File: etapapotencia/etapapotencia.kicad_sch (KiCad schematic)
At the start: 9 parts

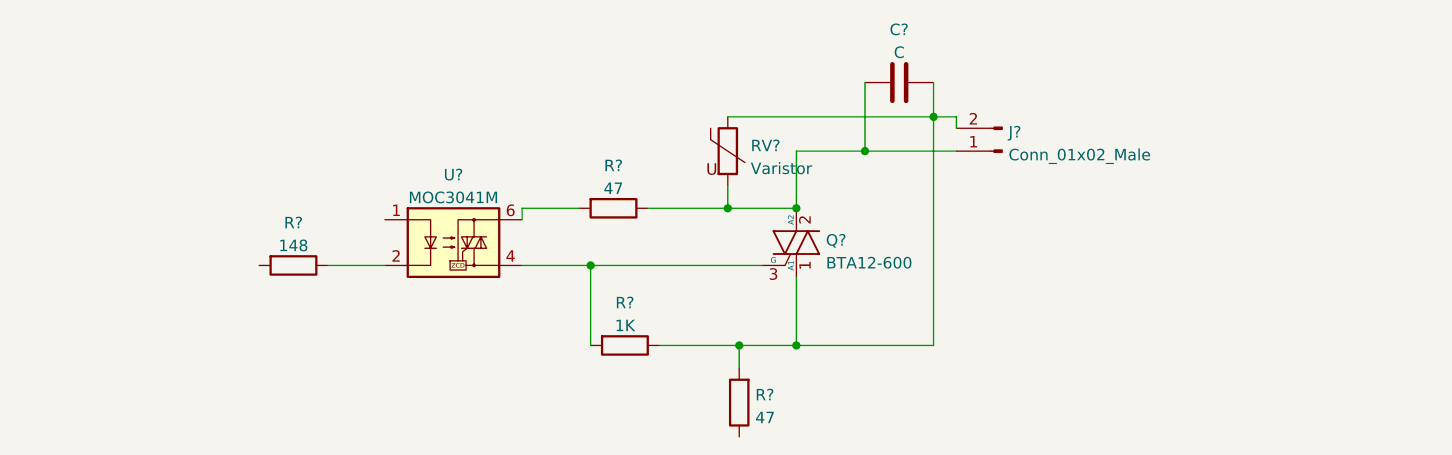
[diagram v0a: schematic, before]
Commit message: Reomo esquemas de etapa de potencia con MOc
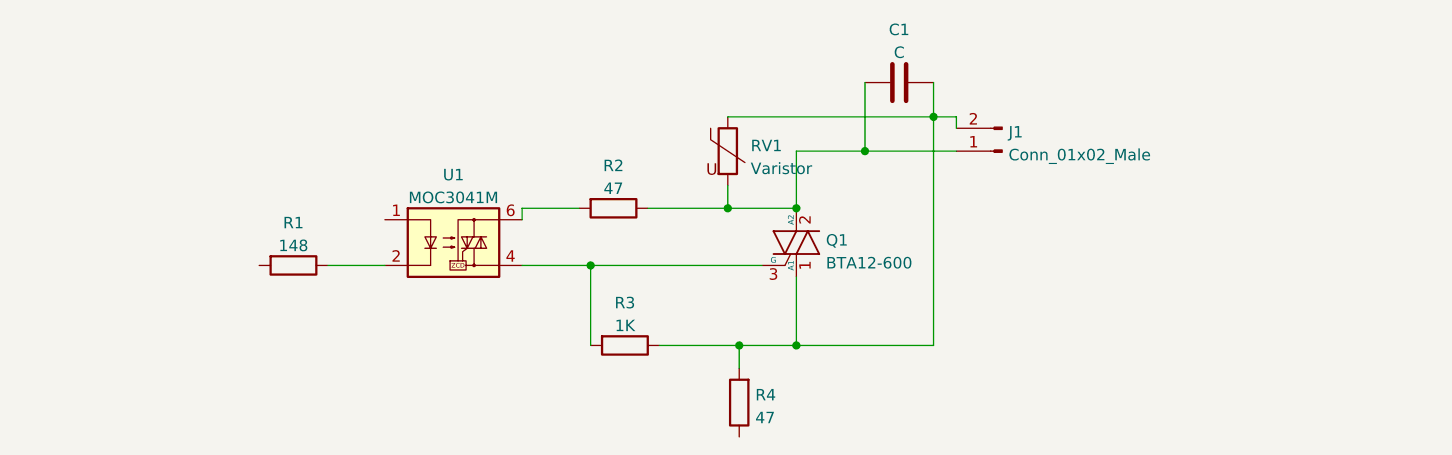
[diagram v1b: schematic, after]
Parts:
- gave numbers to parts that had none: 9
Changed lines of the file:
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@@
   (symbol (lib_id "Device:C") (at 137.16 27.94 90) (unit 1)
     (in_bom yes) (on_board yes) (fields_autoplaced)
-    (property "Reference" "C?" (id 0) (at 137.16 22.0812 90))
+    (property "Reference" "C1" (id 0) (at 137.16 22.0812 90))
     (property "Value" "C" (id 1) (at 137.16 24.6181 90))
     (property "Footprint" "" (id 2) (at 140.97 26.9748 0)
@@
   (symbol (lib_id "Device:R") (at 119.38 63.5 180) (unit 1)
     (in_bom yes) (on_board yes) (fields_autoplaced)
-    (property "Reference" "R?" (id 0) (at 121.158 62.6653 0)
+    (property "Reference" "R4" (id 0) (at 121.158 62.6653 0)
       (effects (font (size 1.27 1.27)) (justify right))
     )
@@
   (symbol (lib_id "Device:R") (at 106.68 57.15 270) (unit 1)
     (in_bom yes) (on_board yes) (fields_autoplaced)
-    (property "Reference" "R?" (id 0) (at 106.68 52.4342 90))
+    (property "Reference" "R3" (id 0) (at 106.68 52.4342 90))
     (property "Value" "1K" (id 1) (at 106.68 54.9711 90))
     (property "Footprint" "" (id 2) (at 106.68 55.372 90)
@@
   (symbol (lib_id "Device:R") (at 105.41 41.91 270) (unit 1)
     (in_bom yes) (on_board yes) (fields_autoplaced)
-    (property "Reference" "R?" (id 0) (at 105.41 37.1942 90))
+    (property "Reference" "R2" (id 0) (at 105.41 37.1942 90))
     (property "Value" "47" (id 1) (at 105.41 39.7311 90))
     (property "Footprint" "" (id 2) (at 105.41 40.132 90)
@@
   (symbol (lib_id "Device:R") (at 69.85 48.26 270) (unit 1)
     (in_bom yes) (on_board yes) (fields_autoplaced)
-    (property "Reference" "R?" (id 0) (at 69.85 43.5442 90))
+    (property "Reference" "R1" (id 0) (at 69.85 43.5442 90))
     (property "Value" "148" (id 1) (at 69.85 46.0811 90))
     (property "Footprint" "" (id 2) (at 69.85 46.482 90)
@@
   (symbol (lib_id "Relay_SolidState:MOC3041M") (at 87.63 45.72 0) (unit 1)
     (in_bom yes) (on_board yes) (fields_autoplaced)
-    (property "Reference" "U?" (id 0) (at 87.63 38.2102 0))
+    (property "Reference" "U1" (id 0) (at 87.63 38.2102 0))
     (property "Value" "MOC3041M" (id 1) (at 87.63 40.7471 0))
     (property "Footprint" "" (id 2) (at 82.55 50.8 0)
@@
   (symbol (lib_id "Device:Varistor") (at 118.11 35.56 0) (unit 1)
     (in_bom yes) (on_board yes) (fields_autoplaced)
-    (property "Reference" "RV?" (id 0) (at 120.65 34.9785 0)
+    (property "Reference" "RV1" (id 0) (at 120.65 34.9785 0)
       (effects (font (size 1.27 1.27)) (justify left))
     )
@@
   (symbol (lib_id "Connector:Conn_01x02_Male") (at 148.59 35.56 180) (unit 1)
     (in_bom yes) (on_board yes) (fields_autoplaced)
-    (property "Reference" "J?" (id 0) (at 149.3012 33.4553 0)
+    (property "Reference" "J1" (id 0) (at 149.3012 33.4553 0)
       (effects (font (size 1.27 1.27)) (justify right))
     )
@@
   (symbol (lib_id "Triac_Thyristor:BTA16-600B") (at 125.73 45.72 0) (unit 1)
     (in_bom yes) (on_board yes) (fields_autoplaced)
-    (property "Reference" "Q?" (id 0) (at 129.0066 45.4695 0)
+    (property "Reference" "Q1" (id 0) (at 129.0066 45.4695 0)
       (effects (font (size 1.27 1.27)) (justify left))
     )
@@
   (symbol_instances
     (path "/442c7c69-6311-4f67-b7ad-57bd83ca12ac"
-      (reference "C?") (unit 1) (value "C") (footprint "")
+      (reference "C1") (unit 1) (value "C") (footprint "")
     )
     (path "/aabbece1-0066-461f-9279-f1135de9281c"
-      (reference "J?") (unit 1) (value "Conn_01x02_Male") (footprint "")
+      (reference "J1") (unit 1) (value "Conn_01x02_Male") (footprint "")
     )
     (path "/d1df3449-f2af-44b2-b925-0a891fdede50"
-      (reference "Q?") (unit 1) (value "BTA12-600") (footprint "Package_TO_SOT_THT:TO-220-3_Vertical")
+      (reference "Q1") (unit 1) (value "BTA12-600") (footprint "Package_TO_SOT_THT:TO-220-3_Vertical")
+    )
+    (path "/78301c42-f3b9-4915-a603-92ae6952065b"
+      (reference "R1") (unit 1) (value "148") (footprint "")
+    )
+    (path "/65760f6f-f6b5-4d4b-9b50-1e864f4a1b19"
+      (reference "R2") (unit 1) (value "47") (footprint "")
+    )
+    (path "/5c517485-d7db-41c1-8f2d-a3207a70b766"
+      (reference "R3") (unit 1) (value "1K") (footprint "")
     )
     (path "/478176c1-a598-4c07-9d36-807d681f9d03"
-      (reference "R?") (unit 1) (value "47") (footprint "")
-    )
-    (path "/5c517485-d7db-41c1-8f2d-a3207a70b766"
-      (reference "R?") (unit 1) (value "1K") (footprint "")
-    )
-    (path "/65760f6f-f6b5-4d4b-9b50-1e864f4a1b19"
-      (reference "R?") (unit 1) (value "47") (footprint "")
-    )
-    (path "/78301c42-f3b9-4915-a603-92ae6952065b"
-      (reference "R?") (unit 1) (value "148") (footprint "")
+      (reference "R4") (unit 1) (value "47") (footprint "")
     )
     (path "/85d172ac-0e0c-40cd-a40e-2880bf60998e"
-      (reference "RV?") (unit 1) (value "Varistor") (footprint "")
+      (reference "RV1") (unit 1) (value "Varistor") (footprint "")
     )
     (path "/7cb1b5d6-64fb-4de1-883a-f24e58b7f0c6"
-      (reference "U?") (unit 1) (value "MOC3041M") (footprint "")
+      (reference "U1") (unit 1) (value "MOC3041M") (footprint "")
     )
   )

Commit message: Display de 7 segementos Version 1
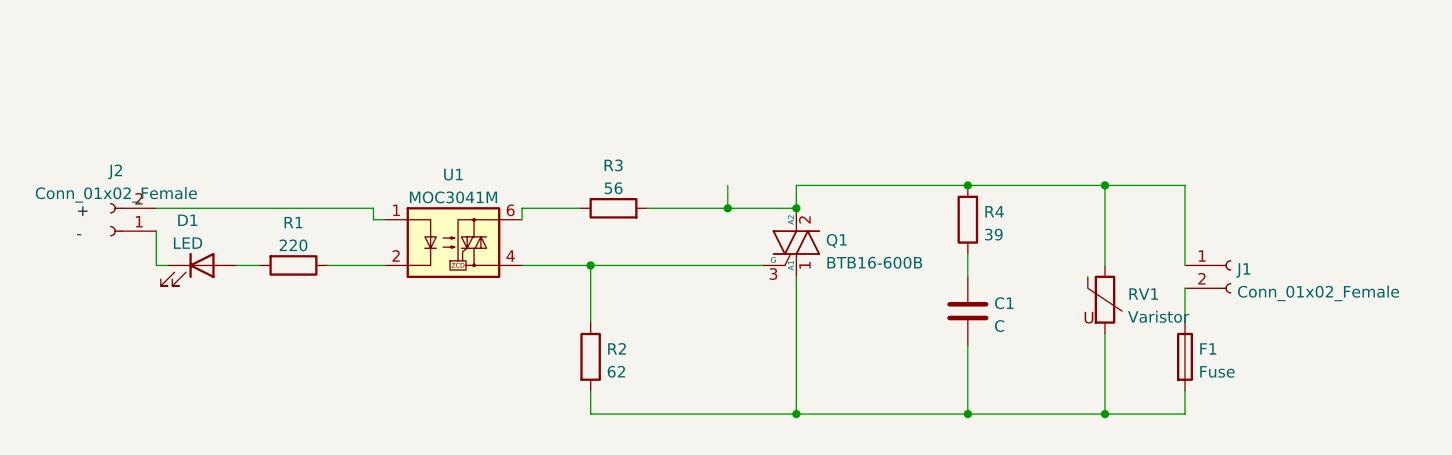
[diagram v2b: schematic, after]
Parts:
- removed J1: Conn_01x02_Male, symbol Connector:Conn_01x02_Male
- removed Q1: BTA12-600, Package_TO_SOT_THT:TO-220-3_Vertical, symbol Triac_Thyristor:BTA16-600B
- added D1: LED, symbol Device:LED
- added F1: Fuse, symbol Device:Fuse
- added J1, J2: Conn_01x02_Female, symbol Connector:Conn_01x02_Female
- added Q1: BTB16-600B, Package_TO_SOT_THT:TO-220-3_Vertical, symbol Triac_Thyristor:BTB16-600B
- R1: value 148 -> 220
- R2: value 47 -> 62
- R3: value 1K -> 56
- R4: value 47 -> 39
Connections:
- net at R4.2, RV1.1: now also R3.2, J1.1 (Pin_1), Q1.2 (A2); no longer C1.2, R3.1
- net at R4.1: now also C1.1
- net at U1.4: now also R2.1, Q1.3 (G); no longer R3.2
- net at R2.2: now also C1.2, RV1.2, F1.2, Q1.1 (A1); no longer U1.6
- net at R1.2: now also D1.2 (A)
- net at U1.1: now also J2.2 (Pin_2)
- new net: D1.1 (K), J2.1 (Pin_1)
- new net: R3.1, U1.6
- new net: F1.1, J1.2 (Pin_2)
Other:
- note added: "+"
- note added: "-"
